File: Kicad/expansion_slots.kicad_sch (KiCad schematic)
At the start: 20 parts, among them J1301 Conn_01x06S, J1302 Neotron-Expansion-Slot, J1303 Neotron-Expansion-Slot, J1304 Neotron-Expansion-Slot, J1305 Neotron-Expansion-Slot, J1306 Conn_01x09, J1307 Conn_01x09, J1308 Conn_01x09

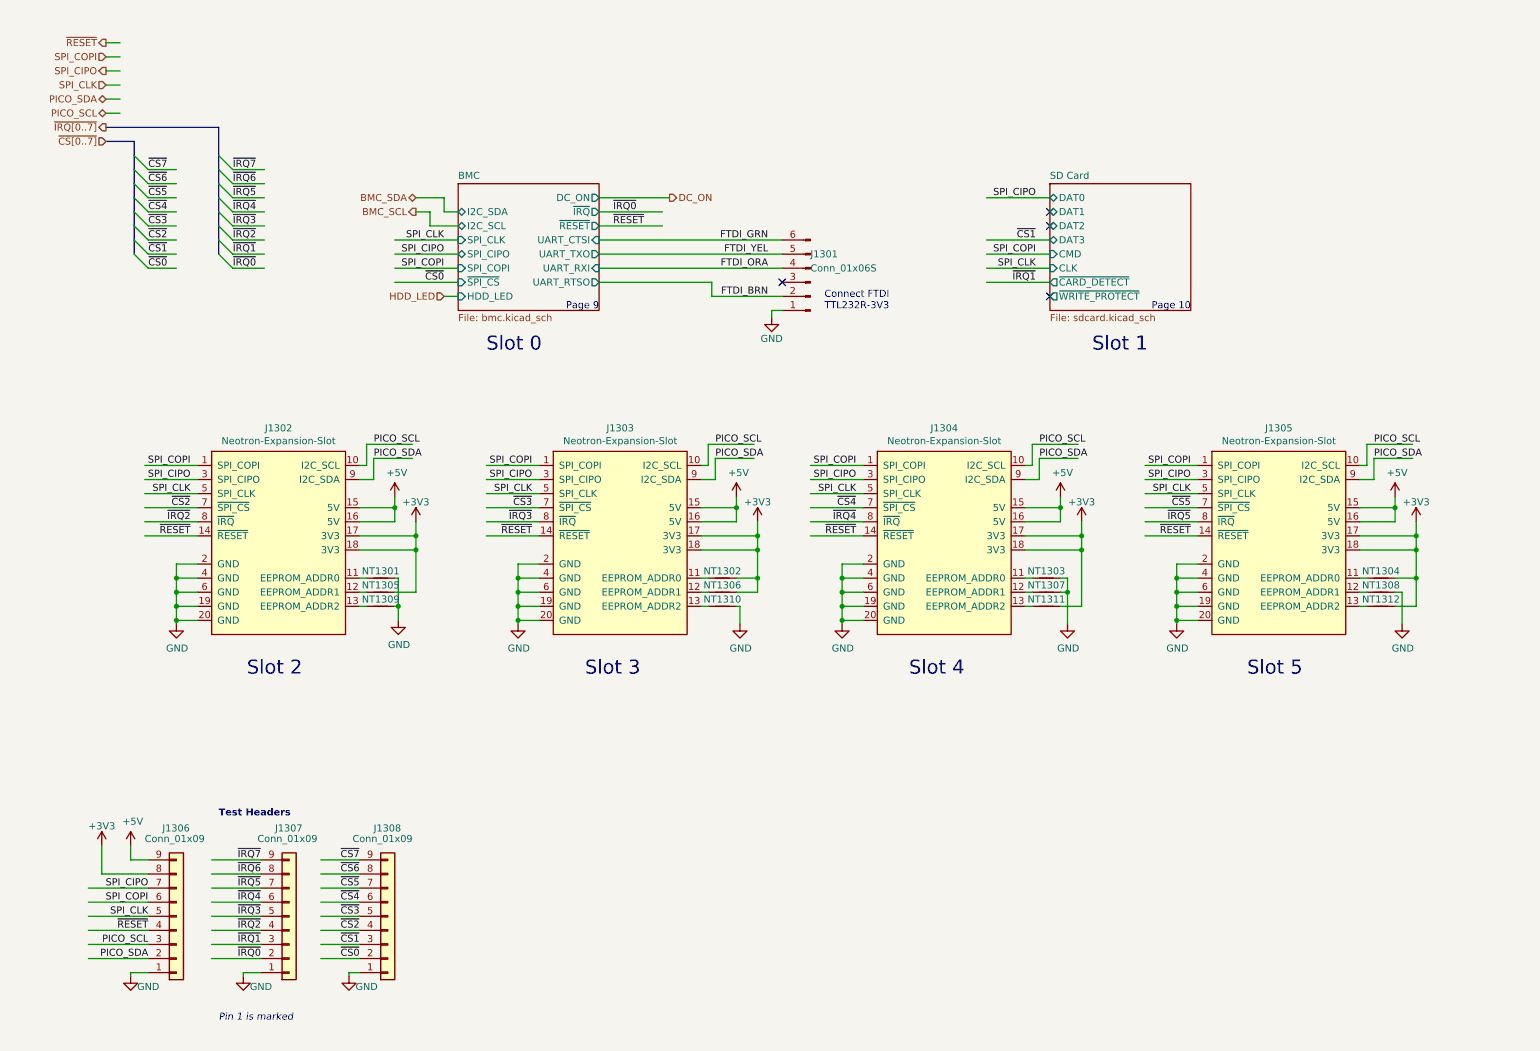
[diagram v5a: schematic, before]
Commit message: Added source resistors on SPI bus.
Also renumbered pages.
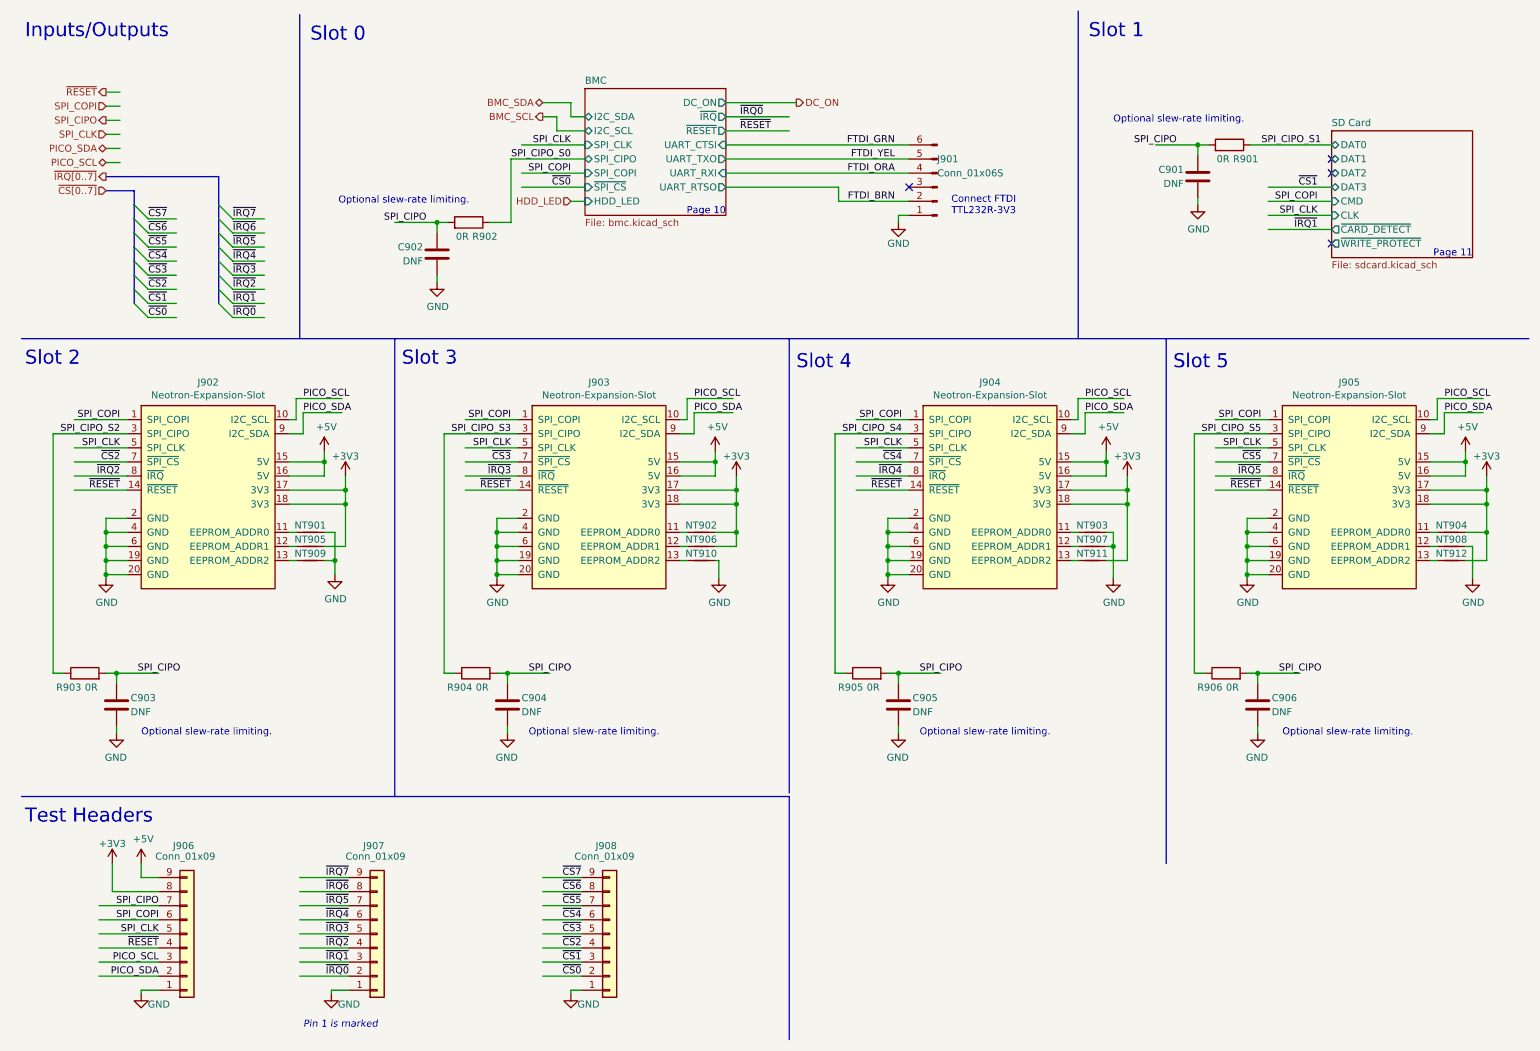
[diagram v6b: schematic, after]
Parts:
- added C901, C902, C903, C904, C905, C906: DNF, Capacitor_SMD:C_0805_2012Metric_Pad1.18x1.45mm_HandSolder, symbol Device:C
- added R901, R902, R903, R904, R905, R906: 0R, Resistor_SMD:R_0805_2012Metric_Pad1.20x1.40mm_HandSolder, symbol Device:R
- renumbered J1301 to J901, J1302 to J902, J1303 to J903, J1304 to J904, J1305 to J905, J1306 to J906, J1307 to J907, J1308 to J908, NT1301 to NT901, NT1302 to NT902, NT1303 to NT903, NT1304 to NT904, NT1305 to NT905, NT1306 to NT906, NT1307 to NT907, NT1308 to NT908, NT1309 to NT909, NT1310 to NT910, NT1311 to NT911, NT1312 to NT912
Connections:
- net GND: now also C901.2, C902.2, C903.2, C904.2, C905.2, C906.2
- net SPI_CIPO: now also C901.1, C902.1, C903.1, C904.1, C905.1, C906.1, R901.2, R902.2, R903.2, R904.2, R905.2, R906.2; no longer J902.3 (SPI_CIPO), J903.3 (SPI_CIPO), J904.3 (SPI_CIPO), J905.3 (SPI_CIPO)
- new net SPI_CIPO_S0: R902.1
- new net SPI_CIPO_S1: R901.1
- new net SPI_CIPO_S2: J902.3 (SPI_CIPO), R903.1
- new net SPI_CIPO_S3: J903.3 (SPI_CIPO), R904.1
- new net SPI_CIPO_S4: J904.3 (SPI_CIPO), R905.1
- new net SPI_CIPO_S5: J905.3 (SPI_CIPO), R906.1
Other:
- note added: "Inputs/Outputs"
- note added: "Optional slew-rate limiting."
- note added: "Page 11"
- note removed: "Page 9"
- moved on the sheet: J901, J902, J903, J904, J905, J906, J907, J908, NT901, NT902, NT903, NT904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

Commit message: Fix net-tie metadata.
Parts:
- NT901, NT902, NT903, NT904, NT905, NT906, NT907, NT908, NT909, NT910, NT911, NT912: DNP (none) -> 1

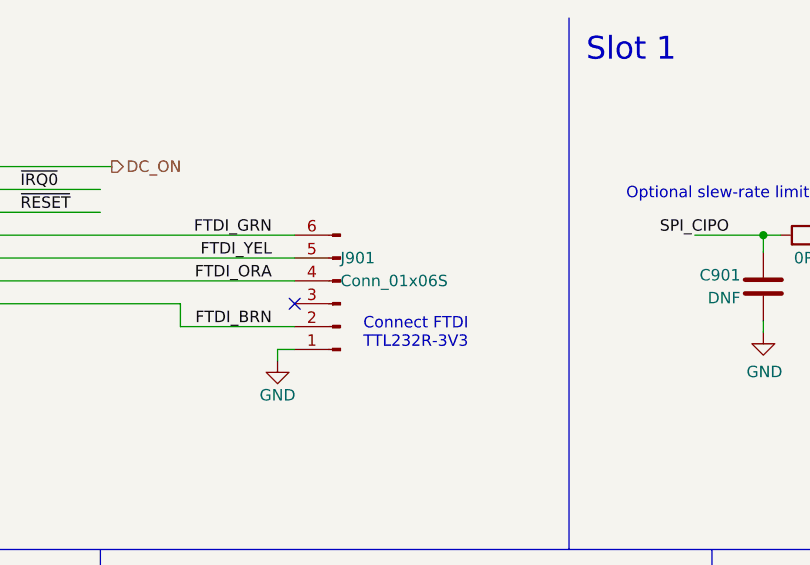
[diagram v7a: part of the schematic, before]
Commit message: Change J901 to be a header not a socket.
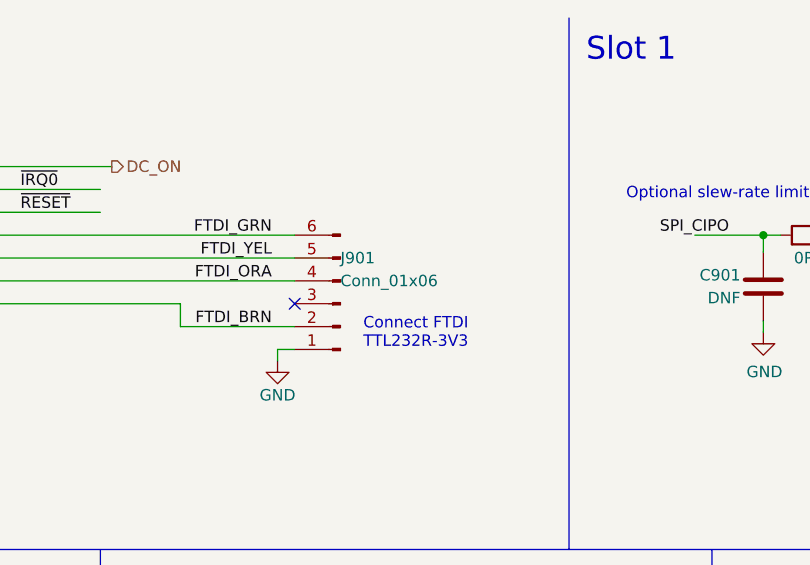
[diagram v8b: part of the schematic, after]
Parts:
- J901: value Conn_01x06S -> Conn_01x06
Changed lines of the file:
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@@
       (effects (font (size 1.27 1.27)) (justify right))
     )
-    (property "Value" "Conn_01x06S" (id 1) (at 177.8 41.275 0)
+    (property "Value" "Conn_01x06" (id 1) (at 177.8 41.275 0)
       (effects (font (size 1.27 1.27)) (justify right))
     )
